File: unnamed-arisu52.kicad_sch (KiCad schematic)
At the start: 0 parts

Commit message: laid out electronics schematic, no footprints assigned
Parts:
- added C1, C2: 22pF, symbol Device:C_Small
- added C3: 1uF, symbol Device:C_Small
- added C4, C5, C6, C7, C8: 0.1uF, symbol Device:C_Small
- added C9: 10uF, symbol Device:C_Small
- added D1, D10, D11, D12, D13, D14, D15, D16, D17, D18, D19, D2, D20, D21, D22, D23, D24, D25, D26, D27, D28, D29, D3, D30, D31, D32, D33, D34, D35, D36, D37, D38, D39, D4, D40, D41, D42, D43, D44, D45, D46, D47, D48, D49, D5, D50, D51, D52, D53, D54, D55, D56, D57, D58, D59, D6, D7, D8, D9: SOD-123, symbol Device:D_Small
- added J1: Conn_01x04_Female, symbol Connector:Conn_01x04_Female
- added MX1, MX10, MX11, MX12, MX13, MX14, MX15, MX16, MX17, MX18, MX19, MX2, MX20, MX21, MX22, MX23, MX24, MX25, MX26, MX27, MX28, MX29, MX3, MX30, MX31, MX32, MX33, MX34, MX35, MX36, MX37, MX38, MX39, MX4, MX40, MX41, MX42, MX43, MX44, MX45, MX46, MX47, MX48, MX49, MX5, MX50, MX51, MX52, MX53, MX54, MX55, MX56, MX57, MX58, MX59, MX6, MX7, MX8, MX9: MX-NoLED, symbol MX_Alps_Hybrid:MX-NoLED
- added R1, R4: 10k, symbol Device:R_Small_US
- added R2, R3: 22k, symbol Device:R_Small_US
- added SW1: SW_Push, symbol Switch:SW_Push
- added U1: ATmega32U4-M, Package_DFN_QFN:QFN-44-1EP_7x7mm_P0.5mm_EP5.2x5.2mm, symbol MCU_Microchip_ATmega:ATmega32U4-M
- added Y1: Crystal_GND24_Small, symbol Device:Crystal_GND24_Small
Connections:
- new net: D14.2 (A), MX14.2 (ROW)
- new net: D39.2 (A), MX39.2 (ROW)
- new net: D20.2 (A), MX20.2 (ROW)
- new net: D12.2 (A), MX12.2 (ROW)
- new net: D22.2 (A), MX22.2 (ROW)
- new net: D57.2 (A), MX57.2 (ROW)
- new net: D43.2 (A), MX43.2 (ROW)
- new net: D37.2 (A), MX37.2 (ROW)
- new net: D25.2 (A), MX25.2 (ROW)
- new net: D8.2 (A), MX8.2 (ROW)
- new net: R2.2, U1.4 (D+)
- new net: D32.2 (A), MX32.2 (ROW)
- new net: D50.2 (A), MX50.2 (ROW)
- new net: D15.2 (A), MX15.2 (ROW)
- new net: D5.2 (A), MX5.2 (ROW)
- new net: D30.2 (A), MX30.2 (ROW)
- new net: R1.2, SW1.2, U1.13 (~{RESET})
- new net: D55.2 (A), MX55.2 (ROW)
- new net: D54.2 (A), MX54.2 (ROW)
- new net: D27.2 (A), MX27.2 (ROW)
- new net: D51.2 (A), MX51.2 (ROW)
- new net: D24.2 (A), MX24.2 (ROW)
- new net: D26.2 (A), MX26.2 (ROW)
- new net: D13.2 (A), MX13.2 (ROW)
- new net: D58.2 (A), MX58.2 (ROW)
- new net: D36.2 (A), MX36.2 (ROW)
- new net: D3.2 (A), MX3.2 (ROW)
- new net: D23.2 (A), MX23.2 (ROW)
- new net: D28.2 (A), MX28.2 (ROW)
- new net: D31.2 (A), MX31.2 (ROW)
- new net: D10.2 (A), MX10.2 (ROW)
- new net: D52.2 (A), MX52.2 (ROW)
- new net: C1.2, U1.17 (XTAL1), Y1.1
- new net: R3.2, U1.3 (D-)
- new net: R4.2, U1.33 (~{HWB}/PE2)
- new net: C3.1, U1.6 (UCAP)
- new net: D48.2 (A), MX48.2 (ROW)
- new net: D21.2 (A), MX21.2 (ROW)
- new net: D49.2 (A), MX49.2 (ROW)
- new net: D46.2 (A), MX46.2 (ROW)
- new net: D16.2 (A), MX16.2 (ROW)
- new net: D33.2 (A), MX33.2 (ROW)
- new net: D40.2 (A), MX40.2 (ROW)
- new net: D7.2 (A), MX7.2 (ROW)
- new net: D59.2 (A), MX59.2 (ROW)
- new net: D45.2 (A), MX45.2 (ROW)
- new net: D44.2 (A), MX44.2 (ROW)
- new net: D2.2 (A), MX2.2 (ROW)
- new net: D17.2 (A), MX17.2 (ROW)
- new net: D56.2 (A), MX56.2 (ROW)
- new net: D42.2 (A), MX42.2 (ROW)
- new net: D38.2 (A), MX38.2 (ROW)
- new net: D41.2 (A), MX41.2 (ROW)
- new net: D34.2 (A), MX34.2 (ROW)
- new net: D11.2 (A), MX11.2 (ROW)
- new net: D1.2 (A), MX1.2 (ROW)
- new net: D4.2 (A), MX4.2 (ROW)
- new net: D6.2 (A), MX6.2 (ROW)
- new net: D47.2 (A), MX47.2 (ROW)
- new net: D19.2 (A), MX19.2 (ROW)
- new net: D35.2 (A), MX35.2 (ROW)
- new net: D29.2 (A), MX29.2 (ROW)
- new net: D18.2 (A), MX18.2 (ROW)
- new net: D53.2 (A), MX53.2 (ROW)
- new net: D9.2 (A), MX9.2 (ROW)
- new net +5V: C4.1, C5.1, C6.1, C7.1, C8.1, C9.1, J1.1 (Pin_1), R1.1, R4.1, U1.14 (VCC), U1.2 (UVCC), U1.24 (AVCC), U1.34 (VCC), U1.44 (AVCC), U1.7 (VBUS)
- new net COL-0: MX1.1 (COL), MX18.1 (COL), MX35.1 (COL)
- new net COL-1: MX19.1 (COL), MX2.1 (COL), MX36.1 (COL), MX52.1 (COL)
- new net COL-10: MX11.1 (COL), MX28.1 (COL), MX45.1 (COL), MX57.1 (COL)
- new net COL-11: MX12.1 (COL), MX29.1 (COL), MX46.1 (COL)
- new net COL-12: MX13.1 (COL), MX30.1 (COL), MX47.1 (COL)
- new net COL-13: MX14.1 (COL), MX31.1 (COL), MX48.1 (COL)
- new net COL-14: MX15.1 (COL), MX32.1 (COL), MX49.1 (COL), MX58.1 (COL)
- new net COL-15: MX16.1 (COL), MX33.1 (COL), MX50.1 (COL)
- new net COL-16: MX17.1 (COL), MX34.1 (COL), MX51.1 (COL), MX59.1 (COL)
- new net COL-2: MX20.1 (COL), MX3.1 (COL), MX37.1 (COL)
- new net COL-3: MX21.1 (COL), MX38.1 (COL), MX4.1 (COL), MX53.1 (COL)
- new net COL-4: MX22.1 (COL), MX39.1 (COL), MX5.1 (COL)
- new net COL-5: MX23.1 (COL), MX40.1 (COL), MX54.1 (COL), MX6.1 (COL)
- new net COL-6: MX24.1 (COL), MX41.1 (COL), MX55.1 (COL), MX7.1 (COL)
- new net COL-7: MX25.1 (COL), MX42.1 (COL), MX8.1 (COL)
- new net COL-8: MX26.1 (COL), MX43.1 (COL), MX56.1 (COL), MX9.1 (COL)
- new net COL-9: MX10.1 (COL), MX27.1 (COL), MX44.1 (COL)
- new net D+: J1.3 (Pin_3), R2.1
- new net D-: J1.2 (Pin_2), R3.1
- new net GND: C1.1, C2.1, C2.2, C3.2, C4.2, C5.2, C6.2, C7.2, C8.2, C9.2, J1.4 (Pin_4), SW1.1, U1.15 (GND), U1.16 (XTAL2), U1.23 (GND), U1.35 (GND), U1.43 (GND), U1.45 (GND), U1.5 (UGND), Y1.2, Y1.3, Y1.4
- new net ROW-0: D1.1 (K), D10.1 (K), D11.1 (K), D12.1 (K), D13.1 (K), D14.1 (K), D15.1 (K), D16.1 (K), D17.1 (K), D2.1 (K), D3.1 (K), D4.1 (K), D5.1 (K), D6.1 (K), D7.1 (K), D8.1 (K), D9.1 (K)
- new net ROW-1: D18.1 (K), D19.1 (K), D20.1 (K), D21.1 (K), D22.1 (K), D23.1 (K), D24.1 (K), D25.1 (K), D26.1 (K), D27.1 (K), D28.1 (K), D29.1 (K), D30.1 (K), D31.1 (K), D32.1 (K), D33.1 (K), D34.1 (K)
- new net ROW-2: D35.1 (K), D36.1 (K), D37.1 (K), D38.1 (K), D39.1 (K), D40.1 (K), D41.1 (K), D42.1 (K), D43.1 (K), D44.1 (K), D45.1 (K), D46.1 (K), D47.1 (K), D48.1 (K), D49.1 (K), D50.1 (K), D51.1 (K)
- new net ROW-3: D52.1 (K), D53.1 (K), D54.1 (K), D55.1 (K), D56.1 (K), D57.1 (K), D58.1 (K), D59.1 (K)
- no-connect marks 0 -> 1

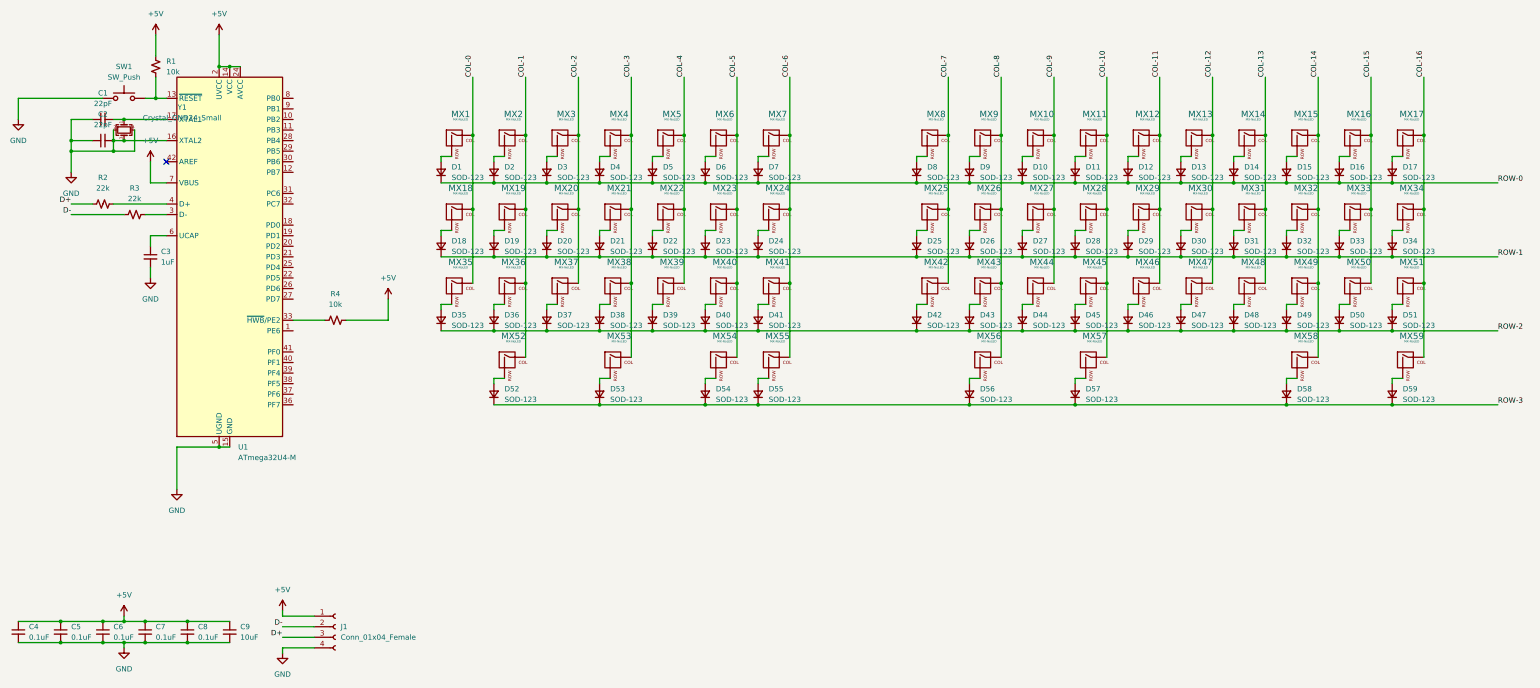
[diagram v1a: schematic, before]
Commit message: resolved some issues with the matrix schematic and laid out the matrix and edge cuts on the pcb
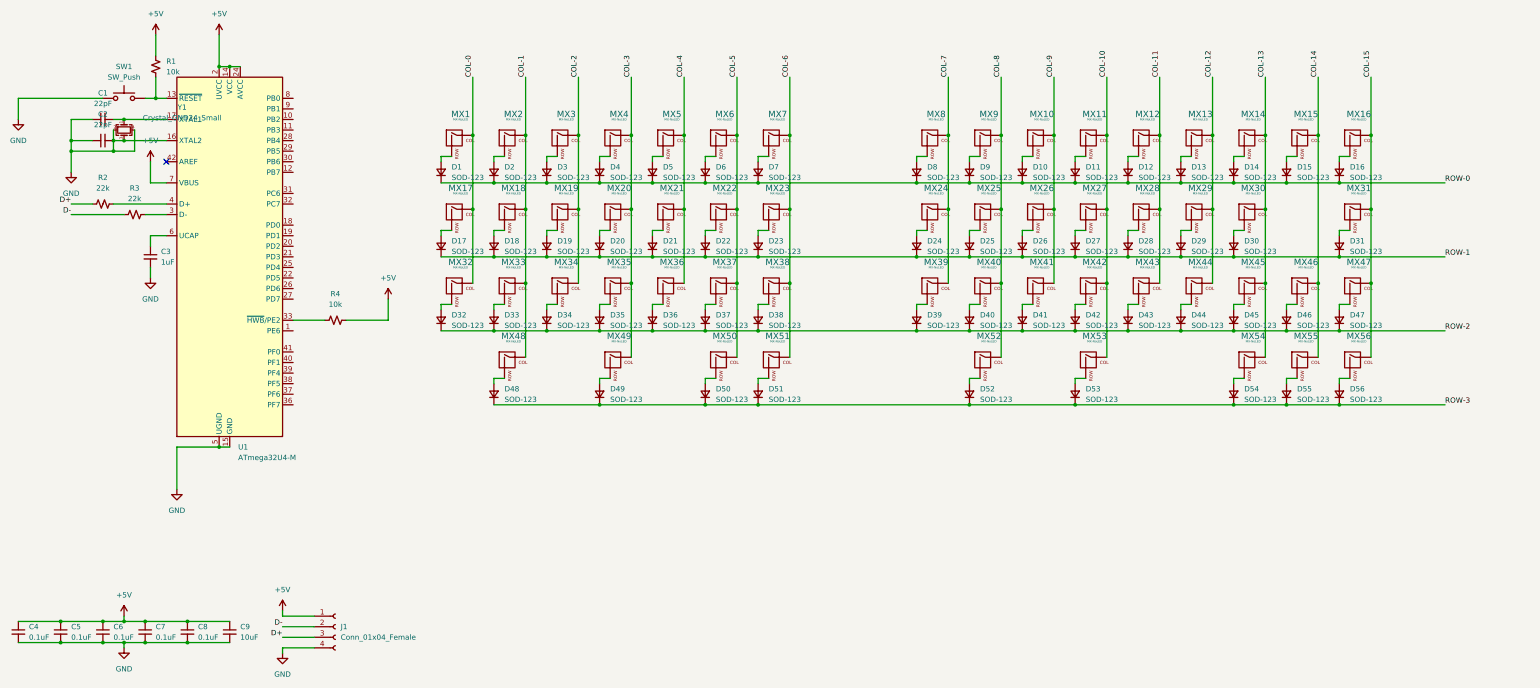
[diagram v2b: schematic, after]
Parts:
- removed D17, D32, D51: SOD-123, symbol Device:D_Small
- removed MX17, MX32, MX50, MX51: MX-NoLED, symbol MX_Alps_Hybrid:MX-NoLED
- added MX55: MX-NoLED, MX_Only:MXOnly-1U-NoLED, symbol MX_Alps_Hybrid:MX-NoLED
- C1, C2, C3, C4, C5, C6, C7, C8, C9: footprint (none) -> Capacitor_SMD:C_0603_1608Metric_Pad1.08x0.95mm_HandSolder
- D1, D10, D11, D12, D13, D14, D15, D16, D2, D3, D4, D5, D6, D7, D8, D9: footprint (none) -> Diode_SMD:D_SOD-123
- D17: renamed from D18; footprint (none) -> Diode_SMD:D_SOD-123
- D18: renamed from D19; footprint (none) -> Diode_SMD:D_SOD-123
- D19: renamed from D20; footprint (none) -> Diode_SMD:D_SOD-123
- D20: renamed from D21; footprint (none) -> Diode_SMD:D_SOD-123
- D21: renamed from D22; footprint (none) -> Diode_SMD:D_SOD-123
- D22: renamed from D23; footprint (none) -> Diode_SMD:D_SOD-123
- D23: renamed from D24; footprint (none) -> Diode_SMD:D_SOD-123
- D24: renamed from D25; footprint (none) -> Diode_SMD:D_SOD-123
- D25: renamed from D26; footprint (none) -> Diode_SMD:D_SOD-123
- D26: renamed from D27; footprint (none) -> Diode_SMD:D_SOD-123
- D27: renamed from D28; footprint (none) -> Diode_SMD:D_SOD-123
- D28: renamed from D29; footprint (none) -> Diode_SMD:D_SOD-123
- D29: renamed from D30; footprint (none) -> Diode_SMD:D_SOD-123
- D30: renamed from D31; footprint (none) -> Diode_SMD:D_SOD-123
- D31: renamed from D34; footprint (none) -> Diode_SMD:D_SOD-123
- D32: renamed from D35; footprint (none) -> Diode_SMD:D_SOD-123
- D33: renamed from D36; footprint (none) -> Diode_SMD:D_SOD-123
- D34: renamed from D37; footprint (none) -> Diode_SMD:D_SOD-123
- D35: renamed from D38; footprint (none) -> Diode_SMD:D_SOD-123
- D36: renamed from D39; footprint (none) -> Diode_SMD:D_SOD-123
- D37: renamed from D40; footprint (none) -> Diode_SMD:D_SOD-123
- D38: renamed from D41; footprint (none) -> Diode_SMD:D_SOD-123
- D39: renamed from D42; footprint (none) -> Diode_SMD:D_SOD-123
- D40: renamed from D43; footprint (none) -> Diode_SMD:D_SOD-123
- D41: renamed from D44; footprint (none) -> Diode_SMD:D_SOD-123
- D42: renamed from D45; footprint (none) -> Diode_SMD:D_SOD-123
- D43: renamed from D46; footprint (none) -> Diode_SMD:D_SOD-123
- D44: renamed from D47; footprint (none) -> Diode_SMD:D_SOD-123
- D45: renamed from D48; footprint (none) -> Diode_SMD:D_SOD-123
- D46: renamed from D49; footprint (none) -> Diode_SMD:D_SOD-123
- D47: renamed from D33; footprint (none) -> Diode_SMD:D_SOD-123
- D48: renamed from D52; footprint (none) -> Diode_SMD:D_SOD-123
- D49: renamed from D53; footprint (none) -> Diode_SMD:D_SOD-123
- D50: renamed from D54; footprint (none) -> Diode_SMD:D_SOD-123
- D51: renamed from D55; footprint (none) -> Diode_SMD:D_SOD-123
- D52: renamed from D56; footprint (none) -> Diode_SMD:D_SOD-123
- D53: renamed from D57; footprint (none) -> Diode_SMD:D_SOD-123
- D54: renamed from D58; footprint (none) -> Diode_SMD:D_SOD-123
- D55: renamed from D50; footprint (none) -> Diode_SMD:D_SOD-123
- D56: renamed from D59; footprint (none) -> Diode_SMD:D_SOD-123
- J1: footprint (none) -> acheron_Connectors:SM04B-SRSS-TB(LF)(SN)
- MX1, MX10, MX11, MX12, MX13, MX14, MX16, MX3, MX4, MX5, MX6, MX7, MX8, MX9: footprint (none) -> MX_Only:MXOnly-1U-NoLED
- MX15, MX2: footprint (none) -> MX_Only:MXOnly-1.5U-NoLED
- MX17: renamed from MX18; footprint (none) -> MX_Only:MXOnly-1U-NoLED
- MX18: renamed from MX19; footprint (none) -> MX_Only:MXOnly-1.25U-NoLED
- MX19: renamed from MX20; footprint (none) -> MX_Only:MXOnly-1U-NoLED
- MX20: renamed from MX21; footprint (none) -> MX_Only:MXOnly-1U-NoLED
- MX21: renamed from MX22; footprint (none) -> MX_Only:MXOnly-1U-NoLED
- MX22: renamed from MX23; footprint (none) -> MX_Only:MXOnly-1U-NoLED
- MX23: renamed from MX24; footprint (none) -> MX_Only:MXOnly-1U-NoLED
- MX24: renamed from MX25; footprint (none) -> MX_Only:MXOnly-1U-NoLED
- MX25: renamed from MX26; footprint (none) -> MX_Only:MXOnly-1U-NoLED
- MX26: renamed from MX27; footprint (none) -> MX_Only:MXOnly-1U-NoLED
- MX27: renamed from MX28; footprint (none) -> MX_Only:MXOnly-1U-NoLED
- MX28: renamed from MX29; footprint (none) -> MX_Only:MXOnly-1U-NoLED
- MX29: renamed from MX30; footprint (none) -> MX_Only:MXOnly-1U-NoLED
- MX30: renamed from MX31; footprint (none) -> MX_Only:MXOnly-2.25U-ReversedStabilizers-NoLED
- MX31: renamed from MX34; footprint (none) -> MX_Only:MXOnly-1U-NoLED
- MX32: renamed from MX35; footprint (none) -> MX_Only:MXOnly-1U-NoLED
- MX33: renamed from MX36; footprint (none) -> MX_Only:MXOnly-2.25U-NoLED
- MX34: renamed from MX37; footprint (none) -> MX_Only:MXOnly-1U-NoLED
- MX35: renamed from MX38; footprint (none) -> MX_Only:MXOnly-1U-NoLED
- MX36: renamed from MX39; footprint (none) -> MX_Only:MXOnly-1U-NoLED
- MX37: renamed from MX40; footprint (none) -> MX_Only:MXOnly-1U-NoLED
- MX38: renamed from MX41; footprint (none) -> MX_Only:MXOnly-1U-NoLED
- MX39: renamed from MX42; footprint (none) -> MX_Only:MXOnly-1U-NoLED
- MX40: renamed from MX43; footprint (none) -> MX_Only:MXOnly-1U-NoLED
- MX41: renamed from MX44; footprint (none) -> MX_Only:MXOnly-1U-NoLED
- MX42: renamed from MX45; footprint (none) -> MX_Only:MXOnly-1U-NoLED
- MX43: renamed from MX46; footprint (none) -> MX_Only:MXOnly-1U-NoLED
- MX44: renamed from MX47; footprint (none) -> MX_Only:MXOnly-1U-NoLED
- MX45: renamed from MX48; footprint (none) -> MX_Only:MXOnly-1.75U-NoLED
- MX46: renamed from MX49; footprint (none) -> MX_Only:MXOnly-1U-NoLED
- MX47: renamed from MX33; footprint (none) -> MX_Only:MXOnly-1U-NoLED
- MX48: renamed from MX52; footprint (none) -> MX_Only:MXOnly-1.5U-NoLED
- MX49: renamed from MX53; footprint (none) -> MX_Only:MXOnly-1.5U-NoLED
- MX50: renamed from MX54; footprint (none) -> MX_Only:MXOnly-2U-ReversedStabilizers-NoLED
- MX51: renamed from MX55; footprint (none) -> MX_Only:MXOnly-1U-NoLED
- MX52: renamed from MX56; footprint (none) -> MX_Only:MXOnly-2.75U-ReversedStabilizers-NoLED
- MX53: renamed from MX57; footprint (none) -> MX_Only:MXOnly-1.5U-NoLED
- MX54: renamed from MX58; footprint (none) -> MX_Only:MXOnly-1U-NoLED
- MX56: renamed from MX59; footprint (none) -> MX_Only:MXOnly-1U-NoLED
- R1, R2, R3, R4: footprint (none) -> Resistor_SMD:R_0603_1608Metric_Pad0.98x0.95mm_HandSolder
- SW1: footprint (none) -> random-keyboard-parts:SKQG-1155865
- Y1: footprint (none) -> Crystal:Crystal_SMD_3225-4Pin_3.2x2.5mm_HandSoldering
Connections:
- net COL-16 is gone; now on net COL-15: MX31.1 (COL), MX56.1 (COL)
- net COL-13: now also MX54.1 (COL)
- net COL-14: now also MX55.1 (COL); no longer MX54.1 (COL)
- net ROW-1: no longer D47.1 (K)
- net ROW-2: now also D47.1 (K); no longer D55.1 (K)
- net ROW-3: now also D55.1 (K)
- net at D55.2 (A): now also MX55.2 (ROW)
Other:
- moved on the sheet: D31, D47, D54, D55, D56, MX31, MX47, MX54, MX56

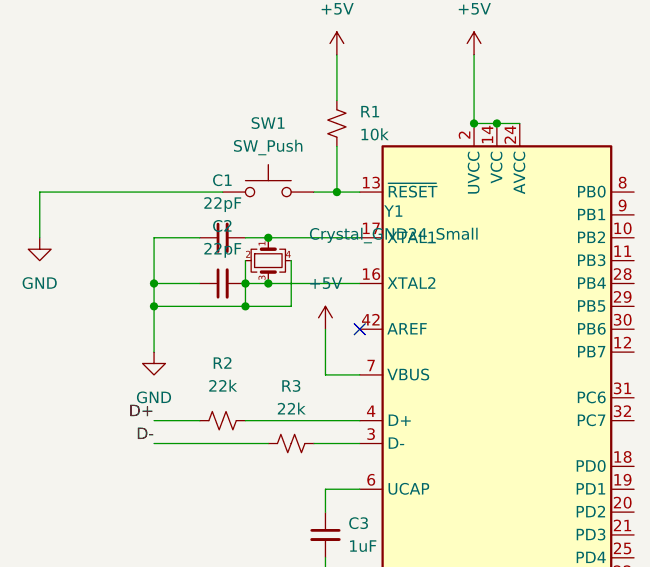
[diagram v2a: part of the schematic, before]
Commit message: routed the matrix
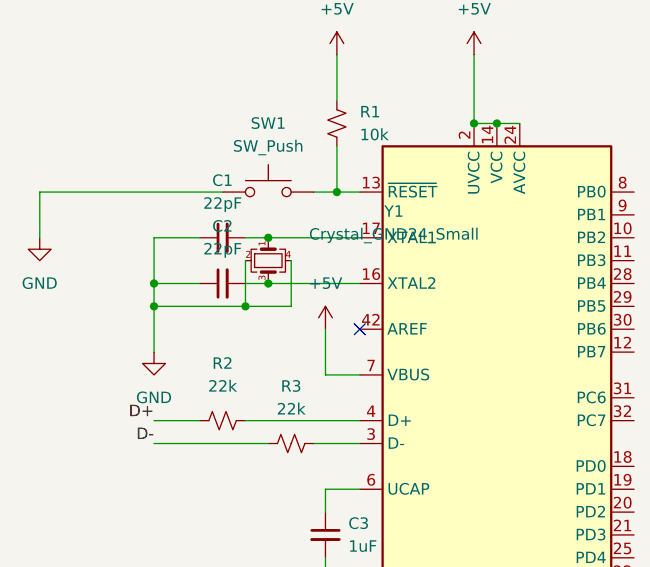
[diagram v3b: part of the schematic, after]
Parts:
- MX50: footprint MX_Only:MXOnly-2U-ReversedStabilizers-NoLED -> MX_Only:MXOnly-2.25U-ReversedStabilizers-NoLED
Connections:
- net GND: no longer C2.2, U1.16 (XTAL2), Y1.3
- new net: C2.2, U1.16 (XTAL2), Y1.3
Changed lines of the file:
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@@
   (junction (at 185.42 69.85) (diameter 0) (color 0 0 0 0)
   )
-  (junction (at 48.26 53.34) (diameter 0) (color 0 0 0 0)
-  )
   (junction (at 160.02 52.07) (diameter 0) (color 0 0 0 0)
   )
@@
     (stroke (width 0) (type default) (color 0 0 0 0))
   )
-  (wire (pts (xy 48.26 53.34) (xy 48.26 55.88))
-    (stroke (width 0) (type default) (color 0 0 0 0))
-  )
   (wire (pts (xy 312.42 52.07) (xy 312.42 69.85))
     (stroke (width 0) (type default) (color 0 0 0 0))
@@
     (stroke (width 0) (type default) (color 0 0 0 0))
   )
-  (wire (pts (xy 48.26 50.8) (xy 48.26 53.34))
+  (wire (pts (xy 48.26 50.8) (xy 48.26 55.88))
     (stroke (width 0) (type default) (color 0 0 0 0))
   )
@@
       (effects (font (size 0.508 0.508)))
     )
-    (property "Footprint" "MX_Only:MXOnly-2U-ReversedStabilizers-NoLED" (id 2) (at 178.435 107.315 0)
+    (property "Footprint" "MX_Only:MXOnly-2.25U-ReversedStabilizers-NoLED" (id 2) (at 178.435 107.315 0)
       (effects (font (size 1.524 1.524)) hide)
     )
@@
     )
     (path "/296c2eff-03e3-4fd1-8ca9-38910d17dd21"
-      (reference "MX50") (unit 1) (value "MX-NoLED") (footprint "MX_Only:MXOnly-2U-ReversedStabilizers-NoLED")
+      (reference "MX50") (unit 1) (value "MX-NoLED") (footprint "MX_Only:MXOnly-2.25U-ReversedStabilizers-NoLED")
     )
     (path "/26c31678-1f80-43a8-b12a-878fbbb64c38"

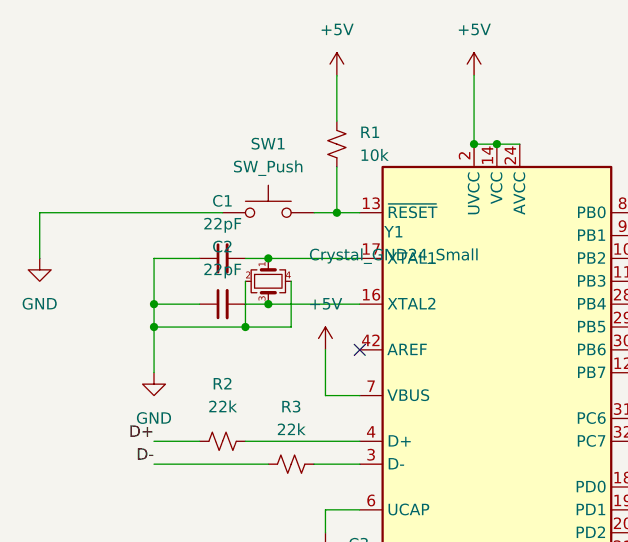
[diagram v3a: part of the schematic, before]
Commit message: started laying out electronics
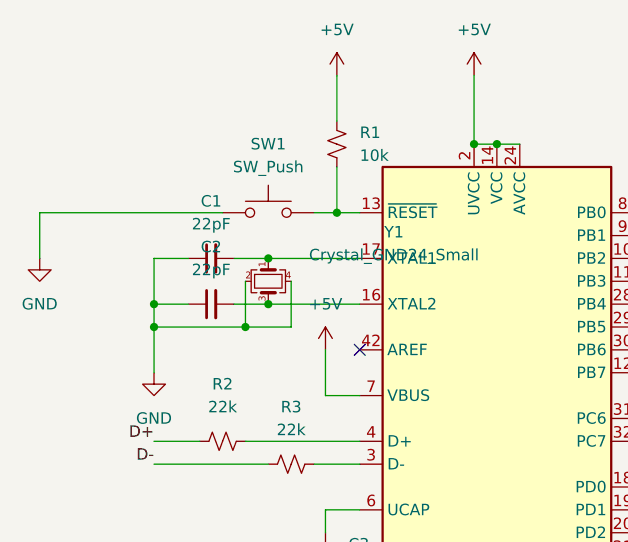
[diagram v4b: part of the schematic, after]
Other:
- moved on the sheet: C1, C2
